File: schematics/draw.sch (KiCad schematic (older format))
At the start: 0 parts

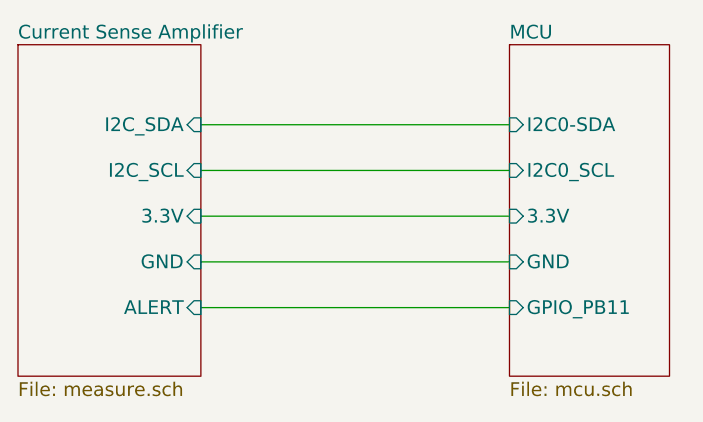
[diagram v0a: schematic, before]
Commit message: added pullups for I2C and alert
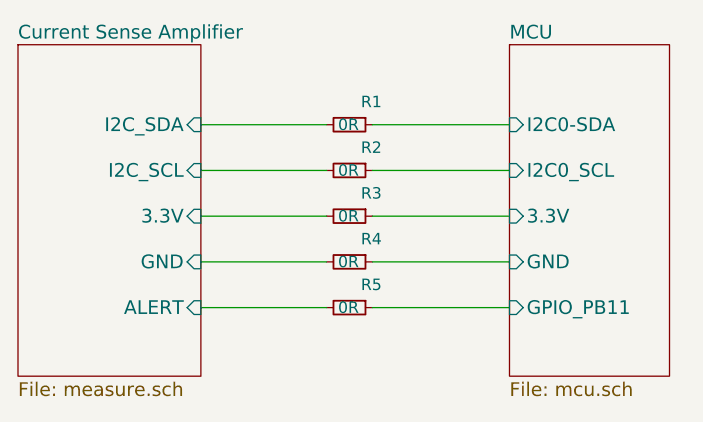
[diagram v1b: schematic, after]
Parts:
- added R1, R2, R3, R4, R5: 0R, Resistors_SMD:R_0805_HandSoldering, symbol R_Small
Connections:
- net Current Sense Amplifier/3.3V: now also R3.2
- net Current Sense Amplifier/ALERT: now also R5.2
- net Current Sense Amplifier/GND: now also R4.2
- net Current Sense Amplifier/I2C_SCL: now also R2.2
- net Current Sense Amplifier/I2C_SDA: now also R1.2
- new net MCU/3.3V: R3.1
- new net MCU/GND: R4.1
- new net MCU/GPIO_PB11: R5.1
- new net MCU/I2C0-SDA: R1.1
- new net MCU/I2C0_SCL: R2.1
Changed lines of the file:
@@
 F6 "ALERT" I R 5150 4400 60
 $EndSheet
+$Comp
+L R_Small R1
+U 1 1 588316A9
+P 5800 3600
+F 0 "R1" V 5700 3650 50  0000 L CNN
+F 1 "0R" V 5800 3550 50  0000 L CNN
+F 2 "Resistors_SMD:R_0805_HandSoldering" H 5800 3600 50  0001 C CNN
+F 3 "" H 5800 3600 50  0000 C CNN
+	1    5800 3600
+	0    1    1    0
+$EndComp
+$Comp
+L R_Small R2
+U 1 1 58831855
+P 5800 3800
+F 0 "R2" V 5700 3850 50  0000 L CNN
+F 1 "0R" V 5800 3750 50  0000 L CNN
+F 2 "Resistors_SMD:R_0805_HandSoldering" H 5800 3800 50  0001 C CNN
+F 3 "" H 5800 3800 50  0000 C CNN
+	1    5800 3800
+	0    1    1    0
+$EndComp
+$Comp
+L R_Small R3
+U 1 1 58831931
+P 5800 4000
+F 0 "R3" V 5700 4050 50  0000 L CNN
+F 1 "0R" V 5800 3950 50  0000 L CNN
+F 2 "Resistors_SMD:R_0805_HandSoldering" H 5800 4000 50  0001 C CNN
+F 3 "" H 5800 4000 50  0000 C CNN
+	1    5800 4000
+	0    1    1    0
+$EndComp
+$Comp
+L R_Small R4
+U 1 1 588319B9
+P 5800 4200
+F 0 "R4" V 5700 4250 50  0000 L CNN
+F 1 "0R" V 5800 4150 50  0000 L CNN
+F 2 "Resistors_SMD:R_0805_HandSoldering" H 5800 4200 50  0001 C CNN
+F 3 "" H 5800 4200 50  0000 C CNN
+	1    5800 4200
+	0    1    1    0
+$EndComp
+$Comp
+L R_Small R5
+U 1 1 58831A3B
+P 5800 4400
+F 0 "R5" V 5700 4450 50  0000 L CNN
+F 1 "0R" V 5800 4350 50  0000 L CNN
+F 2 "Resistors_SMD:R_0805_HandSoldering" H 5800 4400 50  0001 C CNN
+F 3 "" H 5800 4400 50  0000 C CNN
+	1    5800 4400
+	0    1    1    0
+$EndComp
 Wire Wire Line
-	5150 3600 6500 3600
+	6500 3600 5900 3600
 Wire Wire Line
-	5150 3800 6500 3800
+	5700 3600 5150 3600
 Wire Wire Line
-	5150 4000 6500 4000
+	5150 3800 5700 3800
 Wire Wire Line
-	6500 4200 5150 4200
+	5900 3800 6500 3800
 Wire Wire Line
-	5150 4400 6500 4400
+	5150 4000 5700 4000
+Wire Wire Line
+	5900 4000 6500 4000
+Wire Wire Line
+	5150 4400 5700 4400
+Wire Wire Line
+	5900 4400 6500 4400
+Wire Wire Line
+	5900 4200 6500 4200
+Wire Wire Line
+	5700 4200 5150 4200
 $EndSCHEMATC

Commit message: updated to work in kicad 5.1
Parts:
- R1, R2, R3, R4, R5: symbol R_Small -> Device:R_Small
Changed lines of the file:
@@
-EESchema Schematic File Version 2
-LIBS:power
-LIBS:device
-LIBS:transistors
-LIBS:conn
-LIBS:linear
-LIBS:regul
-LIBS:74xx
-LIBS:cmos4000
-LIBS:adc-dac
-LIBS:memory
-LIBS:xilinx
-LIBS:microcontrollers
-LIBS:dsp
-LIBS:microchip
-LIBS:analog_switches
-LIBS:motorola
-LIBS:texas
-LIBS:intel
-LIBS:audio
-LIBS:interface
-LIBS:digital-audio
-LIBS:philips
-LIBS:display
-LIBS:cypress
-LIBS:siliconi
-LIBS:opto
-LIBS:atmel
-LIBS:contrib
-LIBS:valves
-LIBS:draw
-LIBS:switches
-LIBS:silabs
+EESchema Schematic File Version 4
 LIBS:draw-cache
-EELAYER 25 0
+EELAYER 29 0
 EELAYER END
 $Descr A4 11693 8268
@@
 $EndSheet
 $Comp
-L R_Small R1
+L Device:R_Small R1
 U 1 1 588316A9
 P 5800 3600
@@
 $EndComp
 $Comp
-L R_Small R2
+L Device:R_Small R2
 U 1 1 58831855
 P 5800 3800
@@
 $EndComp
 $Comp
-L R_Small R3
+L Device:R_Small R3
 U 1 1 58831931
 P 5800 4000
@@
 $EndComp
 $Comp
-L R_Small R4
+L Device:R_Small R4
 U 1 1 588319B9
 P 5800 4200
@@
 $EndComp
 $Comp
-L R_Small R5
+L Device:R_Small R5
 U 1 1 58831A3B
 P 5800 4400
